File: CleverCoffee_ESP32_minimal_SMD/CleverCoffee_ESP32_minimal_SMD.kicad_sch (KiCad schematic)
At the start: 25 parts

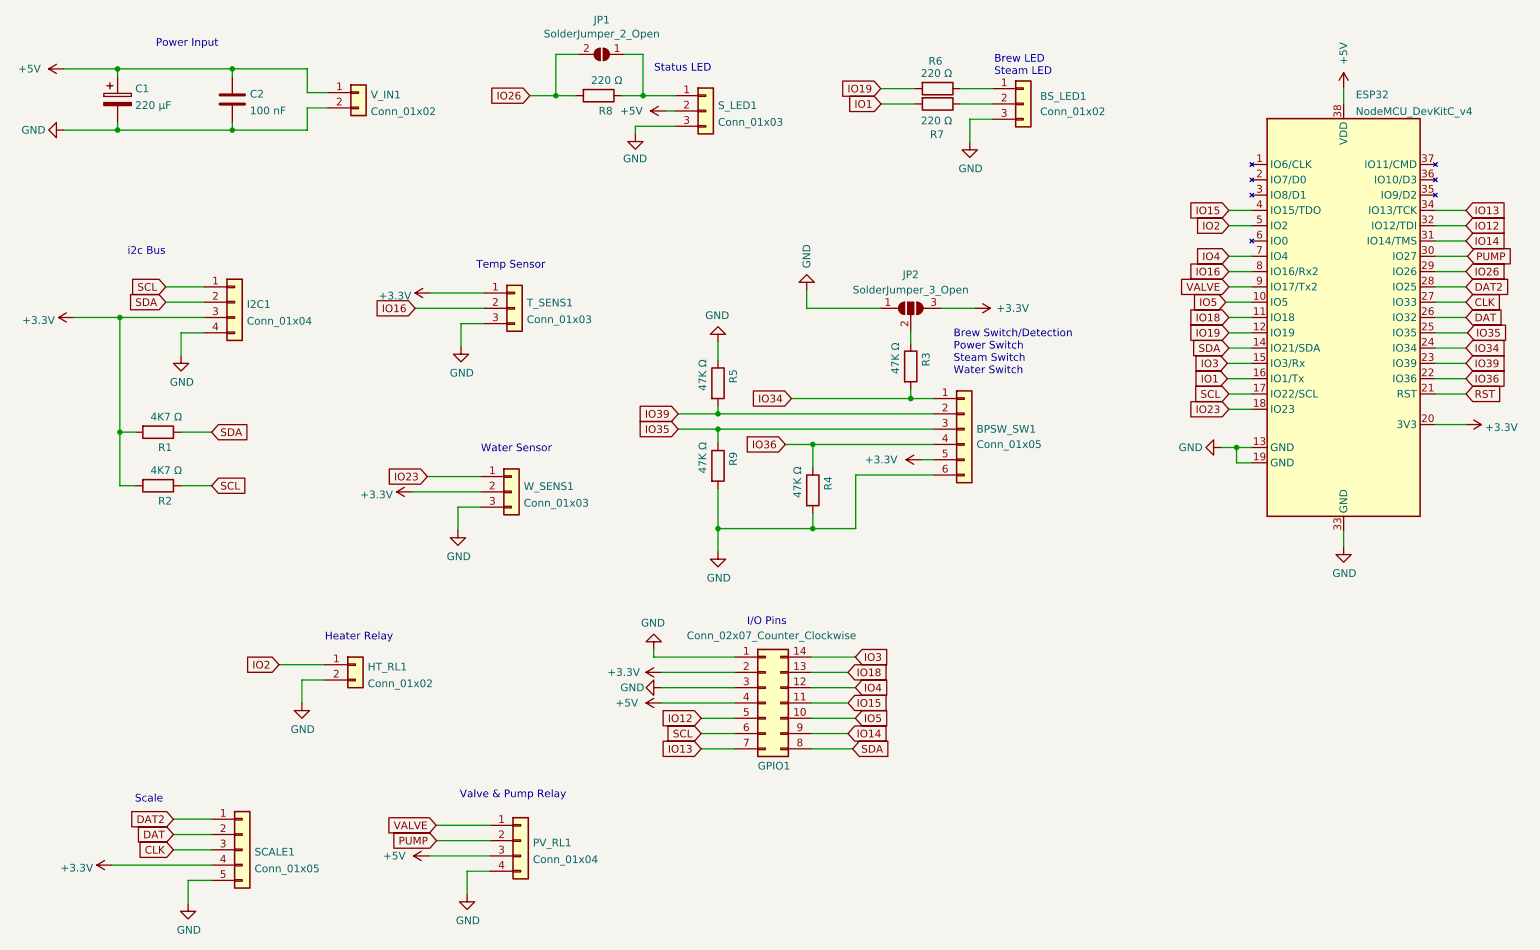
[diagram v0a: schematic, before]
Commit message: mirrored pin headers to correct GND pad, changed SMD footprints to 0805 and rearranged SMD parts
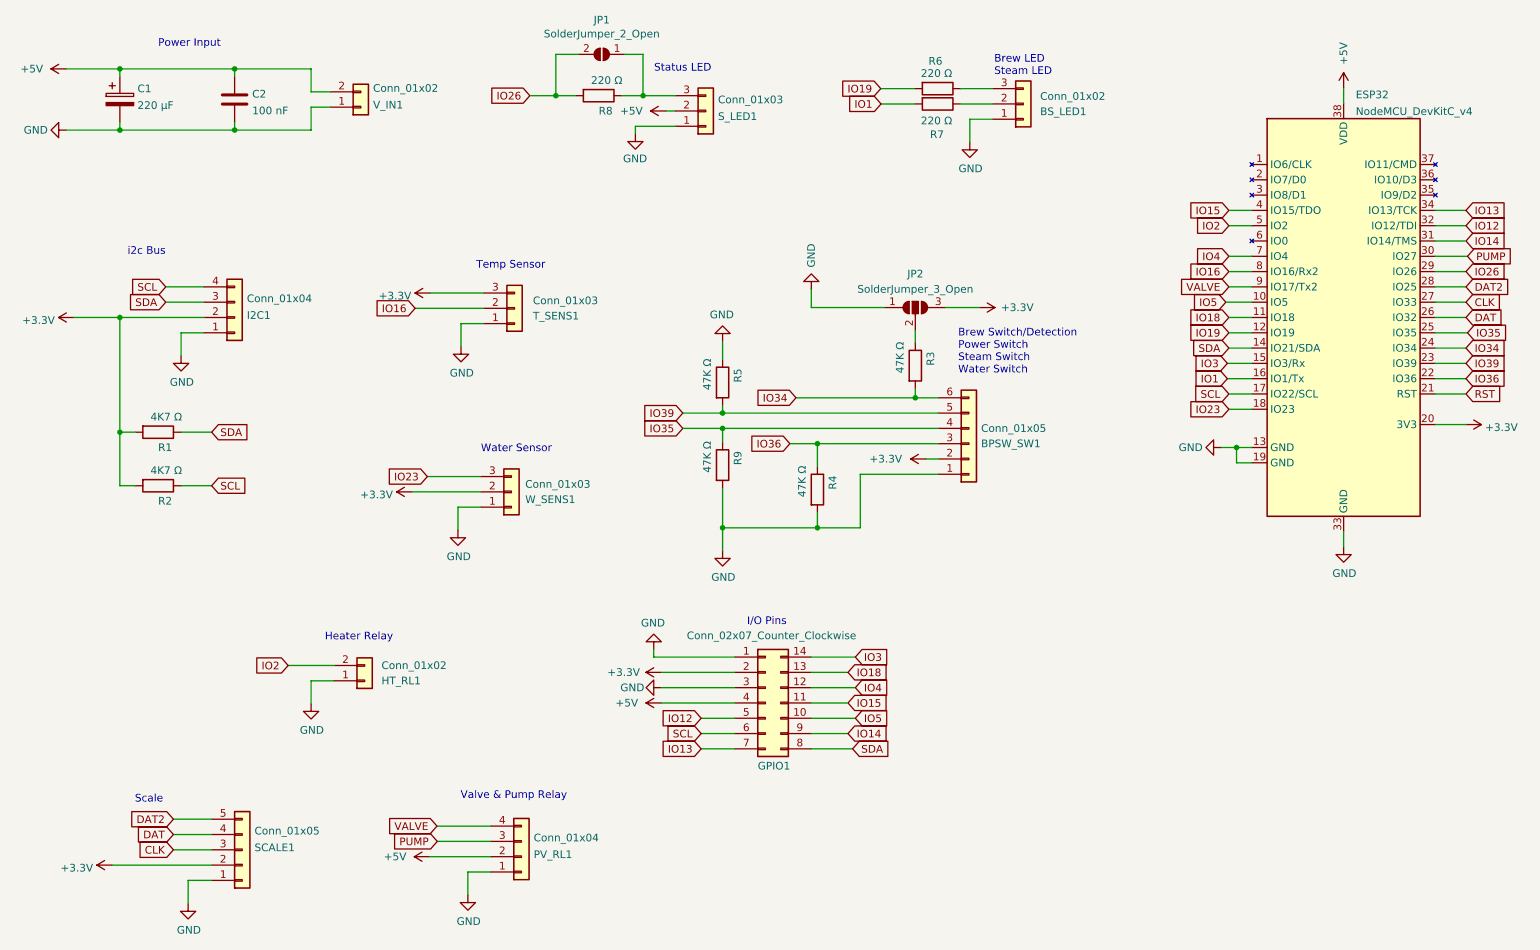
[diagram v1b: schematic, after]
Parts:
- C1: footprint Capacitor_SMD:CP_Elec_6.3x7.7 -> Capacitor_THT:CP_Radial_D6.3mm_P2.50mm
- C2: footprint Capacitor_SMD:C_1206_3216Metric_Pad1.33x1.80mm_HandSolder -> Capacitor_SMD:C_0805_2012Metric_Pad1.18x1.45mm_HandSolder
- R1, R2, R3, R4, R5, R6, R7, R8, R9: footprint Resistor_SMD:R_1206_3216Metric_Pad1.30x1.75mm_HandSolder -> Resistor_SMD:R_0805_2012Metric_Pad1.20x1.40mm_HandSolder
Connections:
- net +3V3: now also BPSW_SW1.2 (Pin_2), I2C1.2 (Pin_2), SCALE1.2 (Pin_2), T_SENS1.3 (Pin_3); no longer BPSW_SW1.5 (Pin_5), I2C1.3 (Pin_3), SCALE1.4 (Pin_4), T_SENS1.1 (Pin_1)
- net +5V: now also PV_RL1.2 (Pin_2), V_IN1.2 (Pin_2); no longer PV_RL1.3 (Pin_3), V_IN1.1 (Pin_1)
- net DAT: now also SCALE1.4 (Pin_4); no longer SCALE1.2 (Pin_2)
- net DAT2: now also SCALE1.5 (Pin_5); no longer SCALE1.1 (Pin_1)
- net GND: now also BPSW_SW1.1 (Pin_1), BS_LED1.1 (Pin_1), HT_RL1.1 (Pin_1), I2C1.1 (Pin_1), PV_RL1.1 (Pin_1), SCALE1.1 (Pin_1), S_LED1.1 (Pin_1), T_SENS1.1 (Pin_1), V_IN1.1 (Pin_1), W_SENS1.1 (Pin_1); no longer BPSW_SW1.6 (Pin_6), BS_LED1.3 (Pin_3), HT_RL1.2 (Pin_2), I2C1.4 (Pin_4), PV_RL1.4 (Pin_4), SCALE1.5 (Pin_5), S_LED1.3 (Pin_3), T_SENS1.3 (Pin_3), V_IN1.2 (Pin_2), W_SENS1.3 (Pin_3)
- net IO2: now also HT_RL1.2 (Pin_2); no longer HT_RL1.1 (Pin_1)
- net IO23: now also W_SENS1.3 (Pin_3); no longer W_SENS1.1 (Pin_1)
- net IO34: now also BPSW_SW1.6 (Pin_6); no longer BPSW_SW1.1 (Pin_1)
- net IO35: now also BPSW_SW1.4 (Pin_4); no longer BPSW_SW1.3 (Pin_3)
- net IO36: now also BPSW_SW1.3 (Pin_3); no longer BPSW_SW1.4 (Pin_4)
- net IO39: now also BPSW_SW1.5 (Pin_5); no longer BPSW_SW1.2 (Pin_2)
- net PUMP: now also PV_RL1.3 (Pin_3); no longer PV_RL1.2 (Pin_2)
- net SCL: now also I2C1.4 (Pin_4); no longer I2C1.1 (Pin_1)
- net SDA: now also I2C1.3 (Pin_3); no longer I2C1.2 (Pin_2)
- net VALVE: now also PV_RL1.4 (Pin_4); no longer PV_RL1.1 (Pin_1)
- net at JP1.1 (A), R8.1: now also S_LED1.3 (Pin_3); no longer S_LED1.1 (Pin_1)
- net at R6.1: now also BS_LED1.3 (Pin_3); no longer BS_LED1.1 (Pin_1)
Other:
- moved on the sheet: BPSW_SW1, HT_RL1, JP2, R3, R4, R5, R9
